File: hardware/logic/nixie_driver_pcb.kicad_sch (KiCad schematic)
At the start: 1 part, among them J3 Conn_02x05_Odd_Even

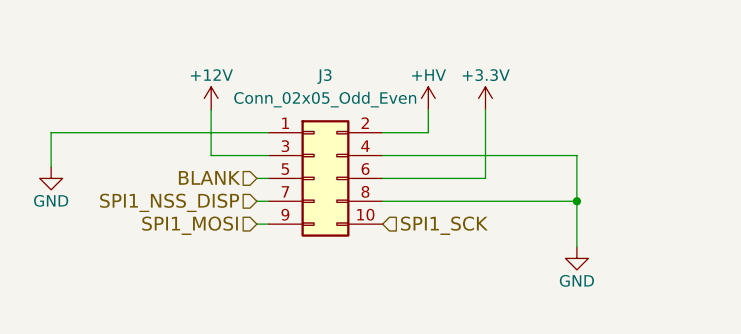
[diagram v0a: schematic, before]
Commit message: Changed connectors to driver board, fixed oscillator connections
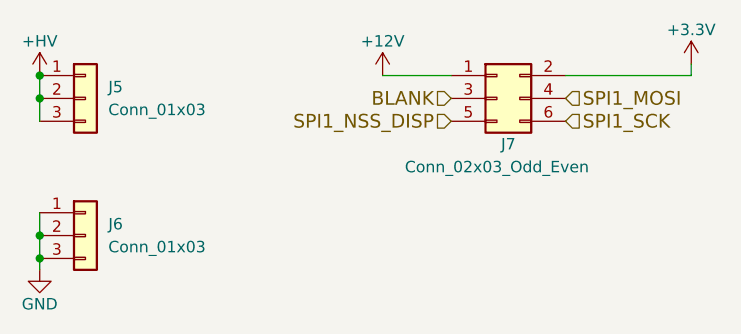
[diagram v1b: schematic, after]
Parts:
- removed J3: Conn_02x05_Odd_Even, Connector_PinSocket_2.54mm:PinSocket_2x05_P2.54mm_Vertical, symbol Connector_Generic:Conn_02x05_Odd_Even
- added J5, J6: Conn_01x03, Connector_PinHeader_2.54mm:PinHeader_1x03_P2.54mm_Vertical, symbol Connector_Generic:Conn_01x03
- added J7: Conn_02x03_Odd_Even, Connector_PinHeader_2.54mm:PinHeader_2x03_P2.54mm_Vertical, symbol Connector_Generic:Conn_02x03_Odd_Even
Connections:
- net +12V: now also J7.1 (Pin_1)
- net +3V3: now also J7.2 (Pin_2)
- net +HV: now also J5.1 (Pin_1), J5.2 (Pin_2), J5.3 (Pin_3)
- net BLANK: now also J7.3 (Pin_3)
- net GND: now also J6.1 (Pin_1), J6.2 (Pin_2), J6.3 (Pin_3)
- net SPI1_MOSI: now also J7.4 (Pin_4)
- net SPI1_NSS_DISP: now also J7.5 (Pin_5)
- net SPI1_SCK: now also J7.6 (Pin_6)
